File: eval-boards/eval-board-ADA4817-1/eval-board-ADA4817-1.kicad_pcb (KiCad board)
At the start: 2 copper layers, 36 parts, among them U1 ADA4817-1

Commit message: update-version
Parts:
- moved REF** 0.90 mm to (107.3, 132.1)
- moved REF** 0.90 mm to (156.8, 103.5)
- moved REF** 0.90 mm to (107.3, 103.5)
- moved REF** 0.63 mm to (156.8, 132.1)
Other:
- board outline added: 58.4 x 37.5 mm
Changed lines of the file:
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@@
   (general
     (thickness 1.6)
-    (drawings 6)
+    (drawings 10)
     (tracks 215)
     (zones 0)
@@
   )
   (setup
-    (last_trace_width 0.4)
+    (last_trace_width 0.25)
     (user_trace_width 0.4)
     (trace_clearance 0.2)
@@
     (solder_mask_min_width 0.25)
     (aux_axis_origin 0 0)
-    (visible_elements FFFFFF7F)
+    (visible_elements 7FFFFFFF)
     (pcbplotparams
-      (layerselection 0x010fc_ffffffff)
+      (layerselection 0x010f0_ffffffff)
       (usegerberextensions false)
       (usegerberattributes false)
@@
   )
   (module MountingHole:MountingHole_3.2mm_M3_ISO14580_Pad (layer F.Cu)
-    (at 106.68 132.715)
+    (at 107.315 132.08)
     (descr "Mounting Hole 3.2mm, M3, ISO14580")
     (tags "mounting hole 3.2mm m3 iso14580")
@@
   )
   (module MountingHole:MountingHole_3.2mm_M3_ISO14580_Pad (layer F.Cu)
-    (at 157.48 132.08)
+    (at 156.845 132.08)
     (descr "Mounting Hole 3.2mm, M3, ISO14580")
     (tags "mounting hole 3.2mm m3 iso14580")
@@
   )
   (module MountingHole:MountingHole_3.2mm_M3_ISO14580_Pad (layer F.Cu)
-    (at 157.48 102.87)
+    (at 156.845 103.505)
     (descr "Mounting Hole 3.2mm, M3, ISO14580")
     (tags "mounting hole 3.2mm m3 iso14580")
@@
   )
   (module MountingHole:MountingHole_3.2mm_M3_ISO14580_Pad (layer F.Cu)
-    (at 106.68 102.87)
+    (at 107.315 103.505)
     (descr "Mounting Hole 3.2mm, M3, ISO14580")
     (tags "mounting hole 3.2mm m3 iso14580")
@@
     )
   )
+  (gr_line (start 102.87 135.255) (end 102.87 136.525) (layer F.SilkS) (width 0.12))
+  (gr_line (start 102.87 99.06) (end 102.87 99.695) (layer F.SilkS) (width 0.12))
+  (gr_line (start 102.87 99.695) (end 102.87 135.255) (layer F.SilkS) (width 0.12))
+  (gr_line (start 102.87 99.06) (end 102.87 136.525) (layer Edge.Cuts) (width 0.05))
+  (gr_line (start 161.29 99.06) (end 102.87 99.06) (layer Edge.Cuts) (width 0.05))
+  (gr_line (start 161.29 136.525) (end 161.29 99.06) (layer Edge.Cuts) (width 0.05))
+  (gr_line (start 102.87 136.525) (end 161.29 136.525) (layer Edge.Cuts) (width 0.05))
   (gr_line (start 161.29 136.525) (end 102.87 136.525) (layer F.SilkS) (width 0.12))
   (gr_line (start 161.29 99.06) (end 161.29 136.525) (layer F.SilkS) (width 0.12))
-  (gr_line (start 102.87 135.255) (end 102.87 136.525) (layer F.SilkS) (width 0.12))
-  (gr_line (start 102.87 99.06) (end 102.87 99.695) (layer F.SilkS) (width 0.12))
   (gr_line (start 161.29 99.06) (end 102.87 99.06) (layer F.SilkS) (width 0.12))
-  (gr_line (start 102.87 99.695) (end 102.87 135.255) (layer F.SilkS) (width 0.12))
   (segment (start 137.968388 115.549112) (end 138.43 115.0875) (width 0.4) (layer F.Cu) (net 1))
   (segment (start 136.41321 117.10429) (end 137.968388 115.549112) (width 0.4) (layer F.Cu) (net 1))
@@
   (via (at 127 114.3) (size 0.8) (drill 0.4) (layers F.Cu B.Cu) (net 2))
   (via (at 109.22 128.27) (size 0.8) (drill 0.4) (layers F.Cu B.Cu) (net 2))
-  (via (at 109.855 128.905) (size 0.8) (drill 0.4) (layers F.Cu B.Cu) (net 2))
+  (via (at 110.49 128.27) (size 0.8) (drill 0.4) (layers F.Cu B.Cu) (net 2))
   (via (at 111.125 129.54) (size 0.8) (drill 0.4) (layers F.Cu B.Cu) (net 2))
   (via (at 112.395 130.175) (size 0.8) (drill 0.4) (layers F.Cu B.Cu) (net 2))

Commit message: second-order_active_filter
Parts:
- turned C10 to 90 degrees
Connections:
- C10 pad 1: /VEE -> GNDREF
- C10 pad 2: GNDREF -> /VEE
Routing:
- net GNDREF: vias 103 -> 102
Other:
- board text added: "ADA4817-1 eval-board"
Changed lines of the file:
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@@
   (general
     (thickness 1.6)
-    (drawings 10)
-    (tracks 215)
+    (drawings 11)
+    (tracks 214)
     (zones 0)
     (modules 36)
@@
     (mod_text_size 1 1)
     (mod_text_width 0.15)
-    (pad_size 1.5 1.5)
+    (pad_size 2.6 1.6)
     (pad_drill 0)
     (pad_to_mask_clearance 0.051)
@@
   )
   (module Capacitor_SMD:CP_Elec_4x5.3 (layer F.Cu)
-    (at 124.46 104.775 270)
+    (at 124.46 104.775 90)
     (descr "SMD capacitor, aluminum electrolytic, Vishay, 4.0x5.3mm")
     (tags "capacitor electrolytic")
@@
       (effects (font (size 0.8 0.8) (thickness 0.12)))
     )
-    (pad 1 smd roundrect (at -1.8 0 270) (size 2.6 1.6) (layers F.Cu F.Paste F.Mask) (roundrect_rratio 0.15625)
+    (pad 1 smd roundrect (at -1.8 0 90) (size 2.6 1.6) (layers F.Cu F.Paste F.Mask) (roundrect_rratio 0.156)
+      (net 2 GNDREF))
+    (pad 2 smd roundrect (at 1.8 0 90) (size 2.6 1.6) (layers F.Cu F.Paste F.Mask) (roundrect_rratio 0.156)
       (net 8 /VEE))
-    (pad 2 smd roundrect (at 1.8 0 270) (size 2.6 1.6) (layers F.Cu F.Paste F.Mask) (roundrect_rratio 0.15625)
-      (net 2 GNDREF))
     (model ${KISYS3DMOD}/Capacitor_SMD.3dshapes/CP_Elec_4x5.3.wrl
       (at (xyz 0 0 0))
@@
       (rotate (xyz 0 0 0))
     )
+  )
+  (gr_text "ADA4817-1 \neval-board\n" (at 146.05 131.445) (layer F.SilkS)
+    (effects (font (size 1 1) (thickness 0.15)))
   )
   (gr_line (start 102.87 135.255) (end 102.87 136.525) (layer F.SilkS) (width 0.12))
@@
   (via (at 127 114.3) (size 0.8) (drill 0.4) (layers F.Cu B.Cu) (net 2))
   (via (at 109.22 128.27) (size 0.8) (drill 0.4) (layers F.Cu B.Cu) (net 2))
-  (via (at 110.49 128.27) (size 0.8) (drill 0.4) (layers F.Cu B.Cu) (net 2))
   (via (at 111.125 129.54) (size 0.8) (drill 0.4) (layers F.Cu B.Cu) (net 2))
   (via (at 112.395 130.175) (size 0.8) (drill 0.4) (layers F.Cu B.Cu) (net 2))

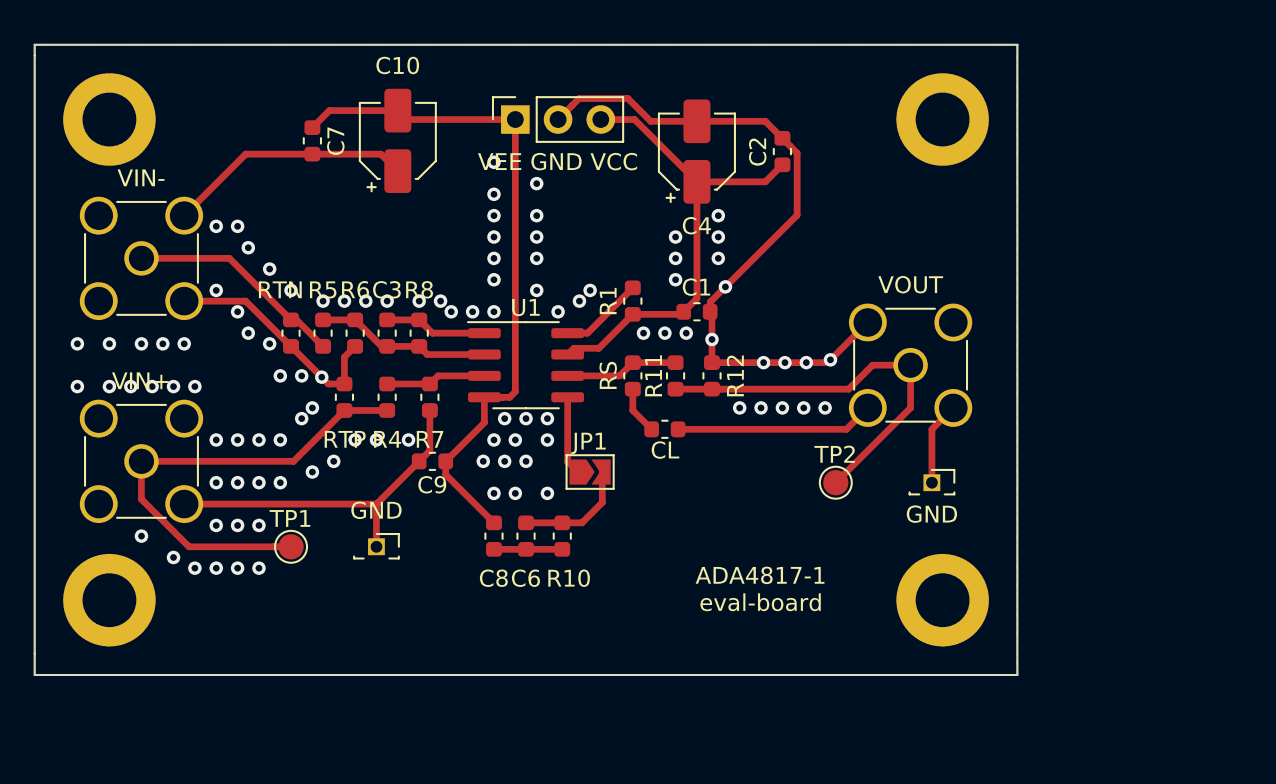
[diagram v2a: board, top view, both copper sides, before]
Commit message: power_and_RF_updated
修正了ADA4817和有源滤波器的电源线管脚、反馈电阻和焊盘handsold
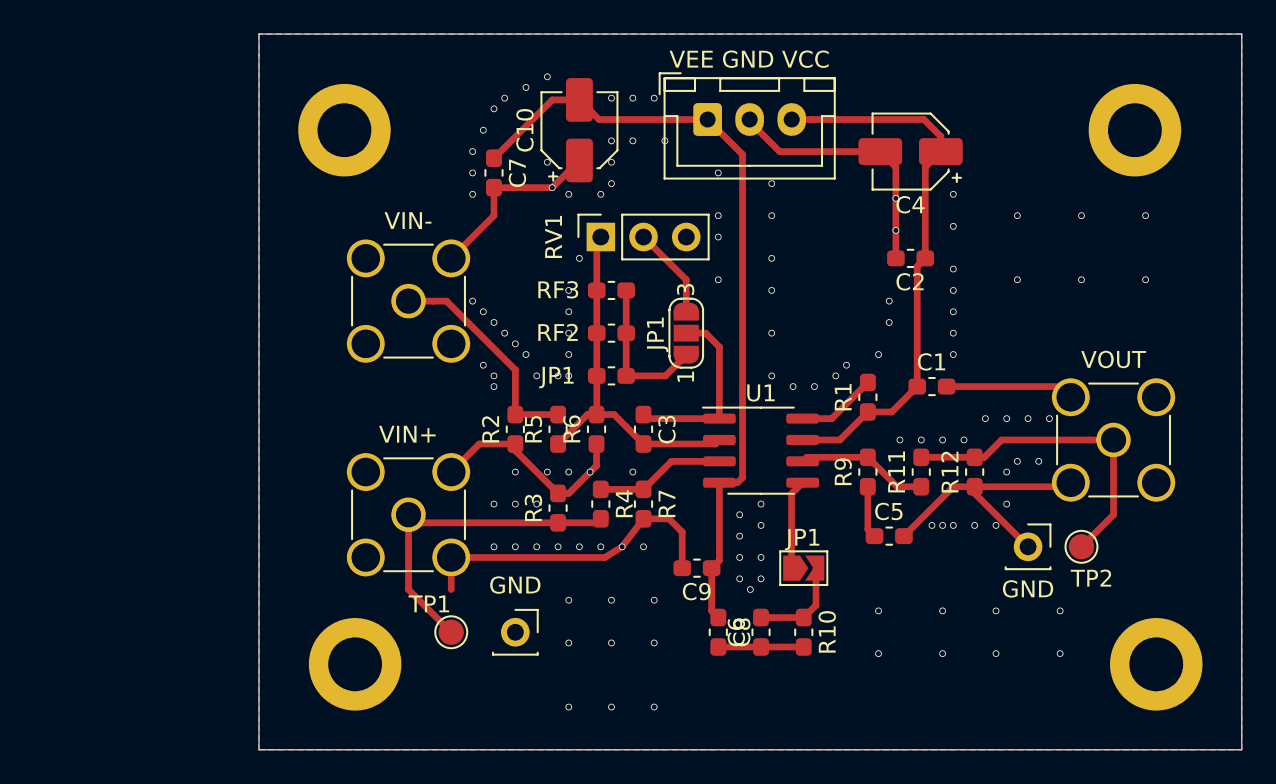
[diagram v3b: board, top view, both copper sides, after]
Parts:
- removed CL: CL, Capacitor_SMD:C_0603_1608Metric
- removed the GND at (156.2, 125.1)
- removed the GND at (123.2, 128.9)
- removed the JP1 at (135.9, 124.5)
- removed R8: RF, Resistor_SMD:R_0603_1608Metric
- removed the REF** at (107.3, 132.1)
- removed the REF** at (156.8, 132.1)
- removed the REF** at (156.8, 103.5)
- removed the REF** at (107.3, 103.5)
- removed RS: RS, Resistor_SMD:R_0603_1608Metric
- removed RTN: RTN, Resistor_SMD:R_0603_1608Metric
- removed RTP: RTP, Resistor_SMD:R_0603_1608Metric
- removed the VEE GND VCC at (131.4, 103.5)
- added C5: CL, Capacitor_SMD:C_0603_1608Metric_Pad1.05x0.95mm_HandSolder, F.Cu at (153.7, 128.3)
- added GND: PinSocket_1x01_P2.54mm_Vertical, Connector_PinSocket_2.54mm:PinSocket_1x01_P2.54mm_Vertical, F.Cu at (131.4, 134.0)
- added GND: PinSocket_1x01_P2.54mm_Vertical, Connector_PinSocket_2.54mm:PinSocket_1x01_P2.54mm_Vertical, F.Cu at (161.9, 128.9)
- added JP1: SolderJumper-2_P1.3mm_Open_TrianglePad1.0x1.5mm, Jumper:SolderJumper-2_P1.3mm_Open_TrianglePad1.0x1.5mm, F.Cu at (148.6, 130.2)
- added JP1: Jumper_3_Open, Jumper:SolderJumper-3_P1.3mm_Open_RoundedPad1.0x1.5mm_NumberLabels, F.Cu at (141.6, 116.2)
- added JP1: R, Resistor_SMD:R_0603_1608Metric_Pad1.05x0.95mm_HandSolder, F.Cu at (137.2, 118.7)
- added R2: RTN, Resistor_SMD:R_0603_1608Metric_Pad1.05x0.95mm_HandSolder, F.Cu at (131.4, 121.9)
- added R3: RTP, Resistor_SMD:R_0603_1608Metric_Pad1.05x0.95mm_HandSolder, F.Cu at (134.0, 126.6)
- added R9: RS, Resistor_SMD:R_0603_1608Metric_Pad1.05x0.95mm_HandSolder, F.Cu at (152.4, 124.5)
- added REF**: MountingHole_3.2mm_M3_ISO14580_Pad, MountingHole:MountingHole_3.2mm_M3_ISO14580_Pad, F.Cu at (168.3, 104.1)
- added REF**: MountingHole_3.2mm_M3_ISO14580_Pad, MountingHole:MountingHole_3.2mm_M3_ISO14580_Pad, F.Cu at (169.5, 135.9)
- added REF**: MountingHole_3.2mm_M3_ISO14580_Pad, MountingHole:MountingHole_3.2mm_M3_ISO14580_Pad, F.Cu at (121.9, 135.9)
- added REF**: MountingHole_3.2mm_M3_ISO14580_Pad, MountingHole:MountingHole_3.2mm_M3_ISO14580_Pad, F.Cu at (121.3, 104.1)
- added RF2: R, Resistor_SMD:R_0603_1608Metric_Pad1.05x0.95mm_HandSolder, F.Cu at (137.2, 116.2)
- added RF3: R, Resistor_SMD:R_0603_1608Metric_Pad1.05x0.95mm_HandSolder, F.Cu at (137.2, 113.7)
- added RV1: R_POT, Connector_PinSocket_2.54mm:PinSocket_1x03_P2.54mm_Vertical, F.Cu at (136.5, 110.5)
- added VEE GND VCC: Conn_01x03_Male, Connector_JST:JST_XH_B3B-XH-A_1x03_P2.50mm_Vertical, F.Cu at (142.9, 103.5)
- C1, C2, C3, C6, C7, C8, C9: footprint Capacitor_SMD:C_0603_1608Metric -> Capacitor_SMD:C_0603_1608Metric_Pad1.05x0.95mm_HandSolder
- C10, C4: footprint Capacitor_SMD:CP_Elec_4x5.3 -> Capacitor_SMD:CP_Elec_4x5.4
- R1, R10, R11, R12, R4, R5, R6, R7: footprint Resistor_SMD:R_0603_1608Metric -> Resistor_SMD:R_0603_1608Metric_Pad1.05x0.95mm_HandSolder
- moved R10 17.5 mm to (148.6, 134.0)
- moved C9 17.0 mm to (142.2, 130.2)
- moved R12 16.6 mm to (158.8, 124.5), turned to 90 degrees
- moved C3 16.3 mm to (139.1, 121.9)
- moved VIN+ 16.2 mm to (125.1, 127.0)
- moved VIN- 16.1 mm to (125.1, 114.3)
- moved R11 15.7 mm to (155.6, 124.5), turned to 90 degrees
- moved R6 15.4 mm to (136.3, 121.9)
- moved R5 15.1 mm to (134.0, 121.9), turned to 90 degrees
- moved R1 15.1 mm to (152.4, 120.0)
- moved TP2 15.1 mm to (165.1, 128.9)
- moved U1 14.9 mm to (146.1, 123.2)
- moved C1 14.7 mm to (156.2, 119.4)
- moved C8 14.5 mm to (143.5, 134.0)
- moved R4 14.2 mm to (136.5, 126.4)
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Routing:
- net GNDREF: track 107.3 -> 82.0 mm, vias 102 -> 127
- net Net-(C3-Pad2): track 10.4 -> 21.8 mm
- net Net-(JP1-Pad1): track 0.00 -> 9.16 mm
- net Net-(J3-Pad1): track 28.2 -> 19.8 mm
- net /VEE: track 40.5 -> 46.6 mm
- net Net-(JP1-Pad3): track 0.00 -> 5.47 mm
- net Net-(C3-Pad1): track 6.11 -> 11.2 mm
- net Net-(J5-Pad1): track 23.4 -> 19.0 mm
- net /VCC: track 28.7 -> 32.9 mm
- net Net-(R4-Pad1): track 5.98 -> 7.74 mm
- net Net-(R11-Pad1): track 6.74 -> 7.87 mm
- net Net-(C6-Pad1): track 4.06 -> 5.08 mm
- net Net-(C6-Pad2): track 11.7 -> 11.1 mm
- net (no net): vias 0 -> 1
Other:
- board size 58.4 x 37.5 mm -> 58.4 x 42.5 mm
- board text removed: "ADA4817-1 eval-board"
